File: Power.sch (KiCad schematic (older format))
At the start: 65 parts, among them J3 ESTOP, J4 PWR, J5 Conn_ARM_JTAG_SWD_10, J7 FAN, Q1 MMBT5401LT1G, Q2 Q_NMOS_GDS, Q3 MMBT3904, Q4 Q_NMOS_GDS, Q5 Q_NMOS_GDS, Q6 Q_NMOS_GDS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

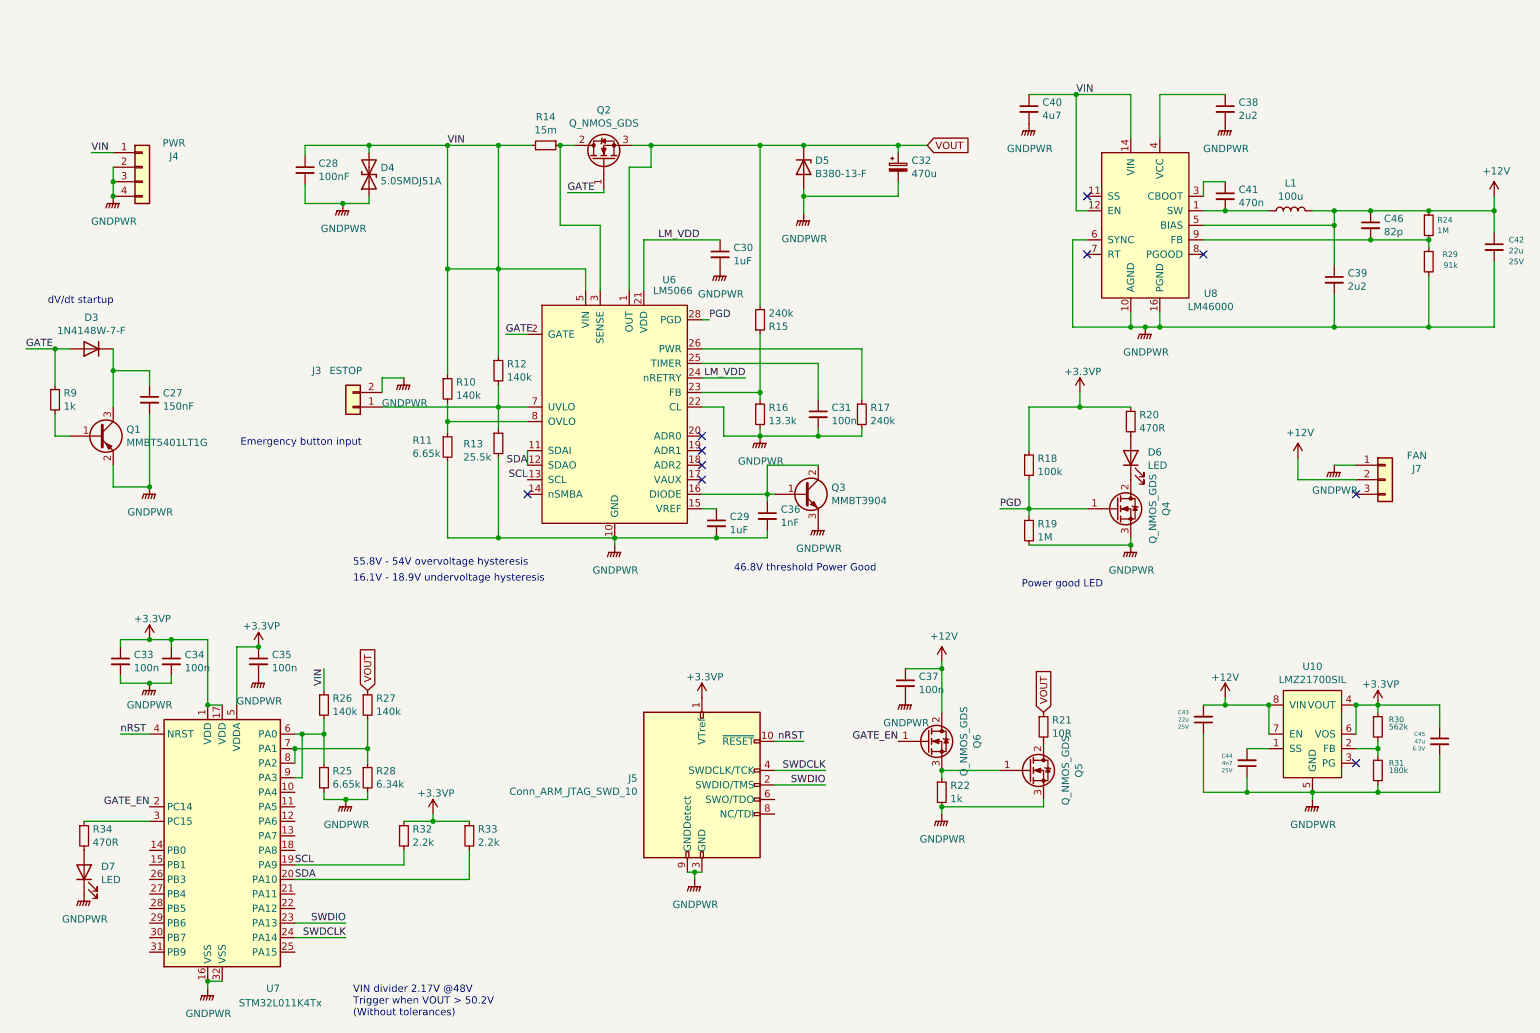
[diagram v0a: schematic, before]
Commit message: add rs485 termination, change to SOT-323 TVS diodes, various OCD
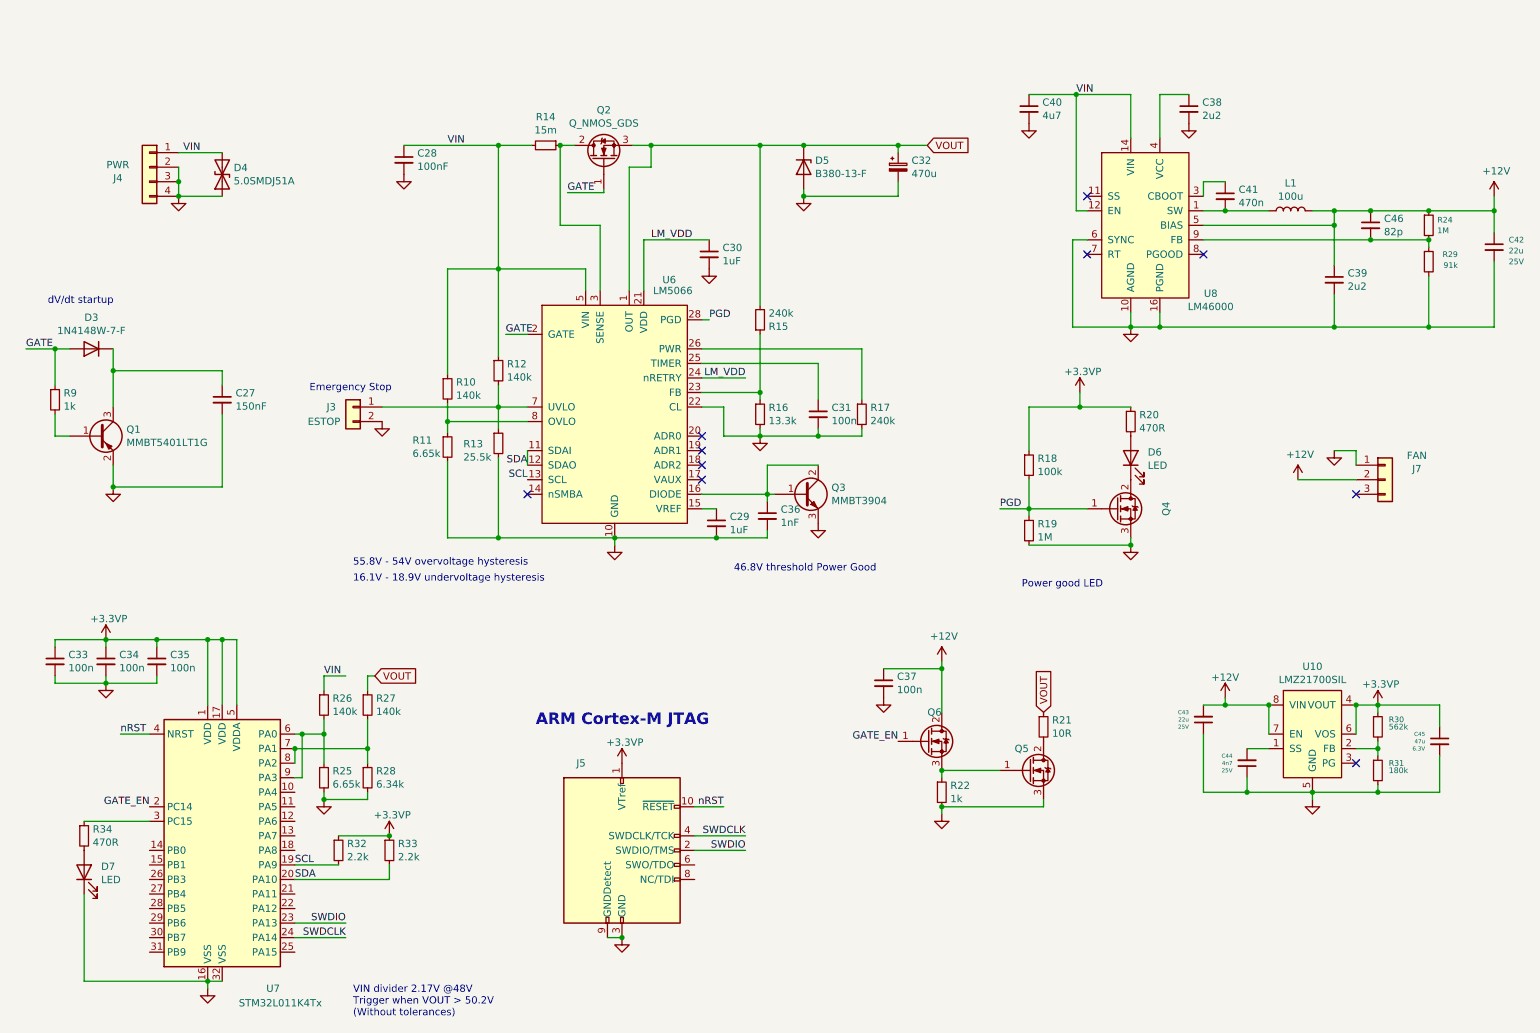
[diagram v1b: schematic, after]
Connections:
- net GNDPWR renamed GND
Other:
- note added: "ARM Cortex-M JTAG"
- note added: "Emergency Stop"
- note removed: "Emergency button input"
- moved on the sheet: C27, C28, C30, C33, C34, C35, C37, C38, D4, J3, J4, J5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

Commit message: working through the power subsystems now. changed e-stop topology.
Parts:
- removed R19: 1M, Resistor_SMD:R_0603_1608Metric, symbol Device:R_Small
- added C47: 100n, Capacitor_SMD:C_0603_1608Metric, symbol Device:C_Small
- added Q7: NTS4001NT1G, Package_TO_SOT_SMD:SOT-323_SC-70, symbol Device:Q_NMOS_GSD
- added R35: 1k, Resistor_SMD:R_0603_1608Metric, symbol Device:R_Small
- added R36: 10k, Resistor_SMD:R_0603_1608Metric, symbol Device:R_Small
- added R37: 100k, Resistor_SMD:R_0603_1608Metric, symbol Device:R_Small
- D4: value 5.0SMDJ51A -> 5.0SMDJ60A; D1N (none) -> Digikey; D1PN (none) -> 5.0SMDJ60ABBCT-ND; MFN (none) -> Bourns; MPN (none) -> 5.0SMDJ60A
- D5: symbol Device:D_Zener -> Device:D_Schottky
- J7: D1N (none) -> digikey; D1PN (none) -> WM4201-ND; MFN (none) -> Molex; MPN (none) -> 0022232031
- R11: value 6.65k -> 6k65
- R13: value 25.5k -> 25k5
- R14: D1N (none) -> Digikey; D1PN (none) -> WSLH-.015CT-ND; MFN (none) -> Vishay Dale; MPN (none) -> WSL2512R0150FEA18
- U6: D1N (none) -> Digikey; D1PN (none) -> 296-LM5066PMHX/NOPBCT-ND; MFN (none) -> TI; MPN (none) -> LM5066PMHX/NOPB
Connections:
- net +12V: now also R35.1
- net GND: now also Q1.3 (C), C47.2, Q7.2 (S), R37.2; no longer J3.2 (Pin_2), Q1.2 (E)
- net at R12.2, R13.1, U6.7 (UVLO): now also Q7.3 (D); no longer J3.1 (Pin_1)
- net at C27.1, D3.1 (K): now also Q1.2 (E); no longer Q1.3 (C)
- new net: J3.1 (Pin_1), R35.2
- new net: C47.1, J3.2 (Pin_2), R36.1
- new net: Q7.1 (G), R36.2, R37.1
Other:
- note added: "COMP1 on PA0/PA1\nCOMP2 on PA3/PA2"
- note added: "I2C addr: ZZZ = 0x40"
- note added: "Schottky diode to eat\nkickback energy at power-off"
- note added: "TODO: check FET pinouts"
- note added: "TODO: check pinout"
- note added: "With a 15 mOhm shunt,\ncurrent limit trips at 3.33 amps (nominal)"
- note added: "open-drain"
- moved on the sheet: C27, C28, C32, C36, D3, D4, D5, J3, J4, J7, Q1, Q2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

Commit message: adding a few notes
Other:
- note added: "20 uA / C27 = 0.133 V / ms ramp rate"
- note added: "TODO: check transistor pinout"
- moved on the sheet: C27, C28, C29, C30, C31, C32, C36, C43, C44, C45, C47, D3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

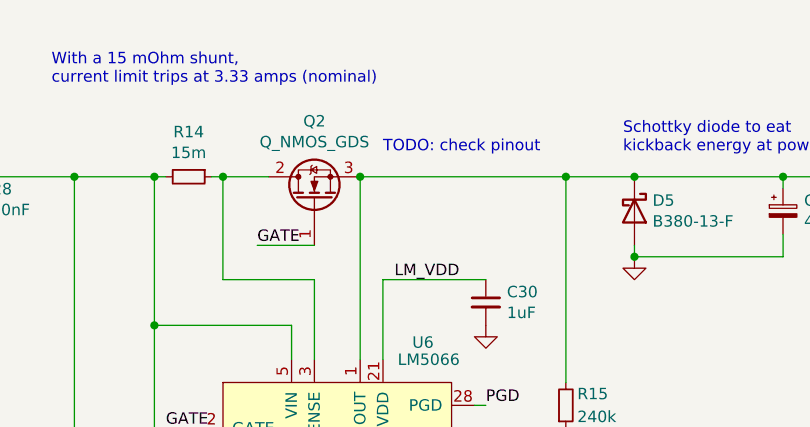
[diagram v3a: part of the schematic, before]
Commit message: add two part numbers
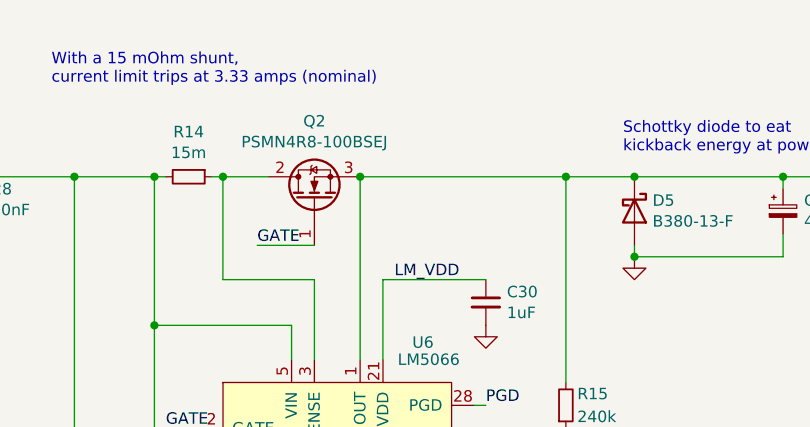
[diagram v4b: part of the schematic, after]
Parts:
- C32: D1N (none) -> Digikey; D1PN (none) -> PCE4859CT-ND; MFN (none) -> Panasonic; MPN (none) -> EEE-FK1K471AM
- D5: D1N (none) -> Digikey; D1PN (none) -> B380-FDICT-ND; MFN (none) -> Diodes Inc; MPN (none) -> B380-13-F
- Q2: value Q_NMOS_GDS -> PSMN4R8-100BSEJ; D1N (none) -> Digikey; D1PN (none) -> 1727-1103-1-ND; MFN (none) -> NXP; MPN (none) -> PSMN4R8-100BSEJ
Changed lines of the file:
@@
 Text Notes 3950 5650 2    50   ~ 0
 COMP1 on PA0/PA1\nCOMP2 on PA3/PA2
-Text Notes 4350 1600 0    50   ~ 0
-TODO: check pinout
 Text Notes 4970 4440 0    50   ~ 0
 46.8V threshold Power Good
@@
 F 2 "Capacitor_SMD:CP_Elec_18x17.5" H 6100 1850 50  0001 C CNN
 F 3 "~" H 6100 1850 50  0001 C CNN
+F 4 "Digikey" H 6100 1850 50  0001 C CNN "D1N"
+F 5 "PCE4859CT-ND" H 6100 1850 50  0001 C CNN "D1PN"
+F 6 "Panasonic" H 6100 1850 50  0001 C CNN "MFN"
+F 7 "EEE-FK1K471AM" H 6100 1850 50  0001 C CNN "MPN"
 	1    6100 1850
 	1    0    0    -1
@@
 F 2 "Diode_SMD:D_SMC" H 5450 1850 50  0001 C CNN
 F 3 "~" H 5450 1850 50  0001 C CNN
+F 4 "Digikey" V 5450 1850 50  0001 C CNN "D1N"
+F 5 "B380-FDICT-ND" V 5450 1850 50  0001 C CNN "D1PN"
+F 6 "Diodes Inc" V 5450 1850 50  0001 C CNN "MFN"
+F 7 "B380-13-F" V 5450 1850 50  0001 C CNN "MPN"
 	1    5450 1850
 	0    1    1    0
@@
 P 4050 1800
 F 0 "Q2" V 4393 1800 50  0000 C CNN
-F 1 "Q_NMOS_GDS" V 4302 1800 50  0000 C CNN
+F 1 "PSMN4R8-100BSEJ" V 4302 1800 50  0000 C CNN
 F 2 "Package_TO_SOT_SMD:TO-263-2" H 4250 1900 50  0001 C CNN
 F 3 "~" H 4050 1800 50  0001 C CNN
+F 4 "Digikey" V 4050 1800 50  0001 C CNN "D1N"
+F 5 "1727-1103-1-ND" V 4050 1800 50  0001 C CNN "D1PN"
+F 6 "NXP" V 4050 1800 50  0001 C CNN "MFN"
+F 7 "PSMN4R8-100BSEJ" V 4050 1800 50  0001 C CNN "MPN"
 	1    4050 1800
 	0    -1   -1   0

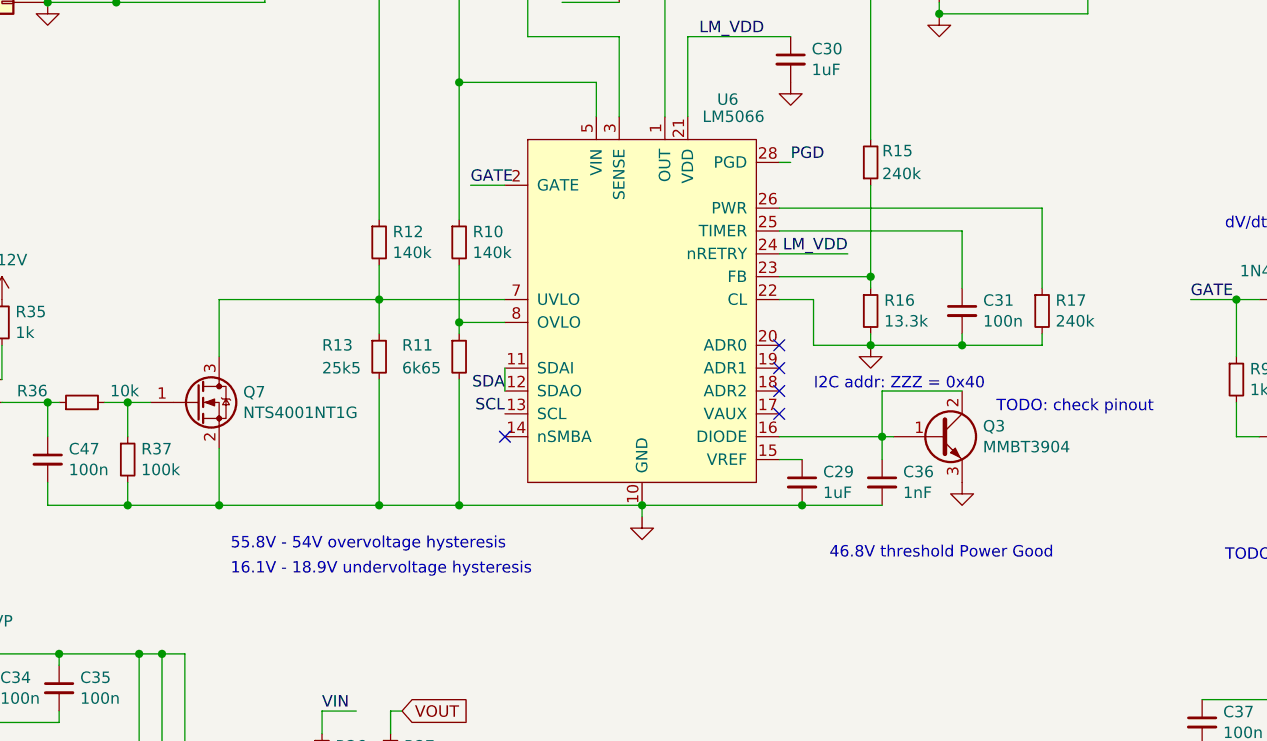
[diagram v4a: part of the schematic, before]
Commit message: recalculate lm5066 passives
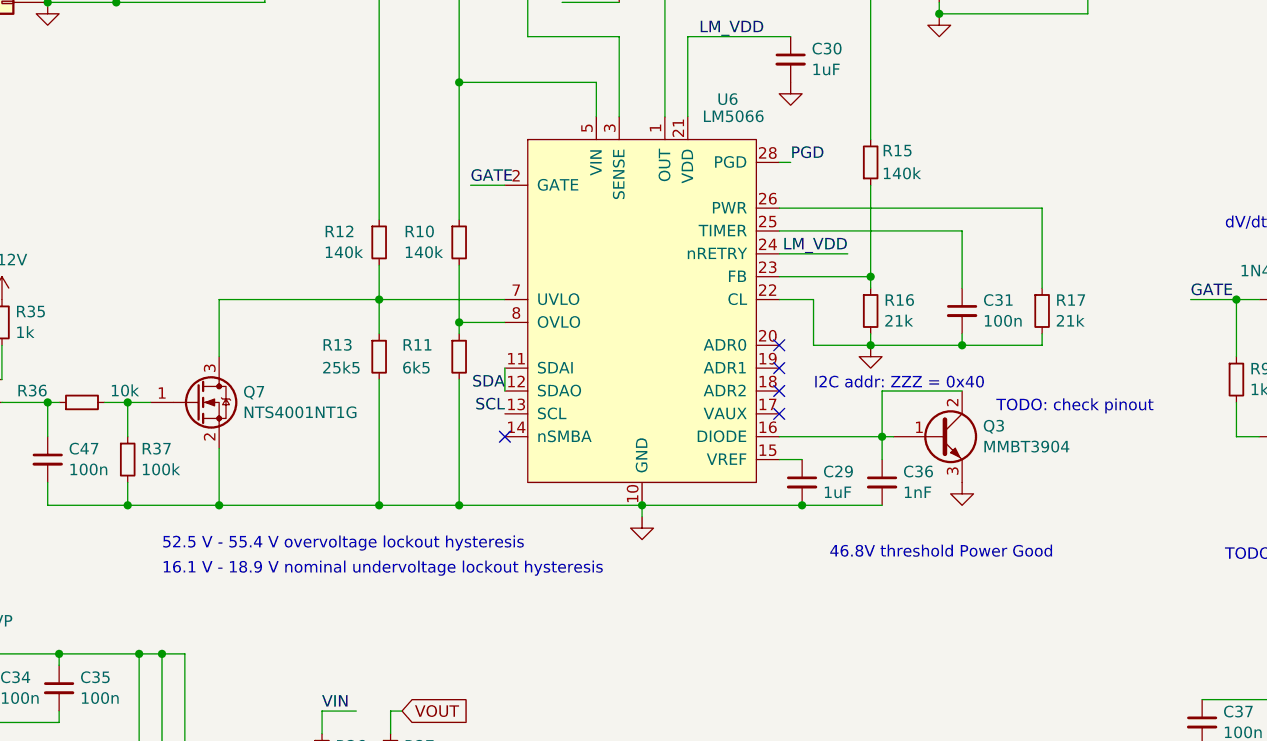
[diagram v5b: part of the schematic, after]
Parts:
- R11: value 6k65 -> 6k5
- R15: value 240k -> 140k
- R16: value 13.3k -> 21k
- R17: value 240k -> 21k
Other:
- note added: "16.1 V - 18.9 V nominal undervoltage lockout hysteresis"
- note added: "52.5 V - 55.4 V overvoltage lockout hysteresis"
- note removed: "16.1V - 18.9V undervoltage hysteresis"
- note removed: "55.8V - 54V overvoltage hysteresis"
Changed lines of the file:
@@
 Text Notes 600  3550 0    50   ~ 0
 Emergency Stop
-Text Notes 2350 4400 0    50   ~ 0
-55.8V - 54V overvoltage hysteresis
-Text Notes 2350 4510 0    50   ~ 0
-16.1V - 18.9V undervoltage hysteresis
+Text Notes 2050 4400 0    50   ~ 0
+52.5 V - 55.4 V overvoltage lockout hysteresis
+Text Notes 2050 4510 0    50   ~ 0
+16.1 V - 18.9 V nominal undervoltage lockout hysteresis
 Text Notes 2900 1300 0    50   ~ 0
 With a 15 mOhm shunt,\ncurrent limit trips at 3.33 amps (nominal)
@@
 U 1 1 5D2C7C82
 P 3000 3050
-F 0 "R12" H 3059 3096 50  0000 L CNN
-F 1 "140k" H 3059 3005 50  0000 L CNN
+F 0 "R12" H 2759 3096 50  0000 L CNN
+F 1 "140k" H 2759 3005 50  0000 L CNN
 F 2 "Resistor_SMD:R_0603_1608Metric" H 3000 3050 50  0001 C CNN
 F 3 "~" H 3000 3050 50  0001 C CNN
@@
 U 1 1 5D2C7C83
 P 3350 3050
-F 0 "R10" H 3409 3096 50  0000 L CNN
-F 1 "140k" H 3409 3005 50  0000 L CNN
+F 0 "R10" H 3109 3096 50  0000 L CNN
+F 1 "140k" H 3109 3005 50  0000 L CNN
 F 2 "Resistor_SMD:R_0603_1608Metric" H 3350 3050 50  0001 C CNN
 F 3 "~" H 3350 3050 50  0001 C CNN
@@
 P 3350 3550
 F 0 "R11" H 3100 3600 50  0000 L CNN
-F 1 "6k65" H 3100 3500 50  0000 L CNN
+F 1 "6k5" H 3100 3500 50  0000 L CNN
 F 2 "Resistor_SMD:R_0603_1608Metric" H 3350 3550 50  0001 C CNN
 F 3 "~" H 3350 3550 50  0001 C CNN
@@
 P 5150 2700
 F 0 "R15" H 5200 2650 50  0000 L CNN
-F 1 "240k" H 5200 2750 50  0000 L CNN
+F 1 "140k" H 5200 2750 50  0000 L CNN
 F 2 "Resistor_SMD:R_0603_1608Metric" H 5150 2700 50  0001 C CNN
 F 3 "~" H 5150 2700 50  0001 C CNN
@@
 P 5150 3350
 F 0 "R16" H 5209 3396 50  0000 L CNN
-F 1 "13.3k" H 5209 3305 50  0000 L CNN
+F 1 "21k" H 5209 3305 50  0000 L CNN
 F 2 "Resistor_SMD:R_0603_1608Metric" H 5150 3350 50  0001 C CNN
 F 3 "~" H 5150 3350 50  0001 C CNN
@@
 P 5900 3350
 F 0 "R17" H 5959 3396 50  0000 L CNN
-F 1 "240k" H 5959 3305 50  0000 L CNN
+F 1 "21k" H 5959 3305 50  0000 L CNN
 F 2 "Resistor_SMD:R_0603_1608Metric" H 5900 3350 50  0001 C CNN
 F 3 "~" H 5900 3350 50  0001 C CNN

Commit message: fix Q3 pinout and chase a few part numbers
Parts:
- D3: D1N (none) -> Digikey; D1PN (none) -> 1N4148W-FDICT-ND; MFN (none) -> Diodes Inc; MPN (none) -> 1N4148W-7-F
- Q1: D1N (none) -> Digikey; D1PN (none) -> MMBT5401LT1GOSCT-ND; MFN (none) -> ON Semi; MPN (none) -> MMBT5401LT1G
- Q3: symbol Device:Q_NPN_BCE -> Device:Q_NPN_BEC; D1N (none) -> Digikey; D1PN (none) -> MMBT3904-FDICT-ND; MFN (none) -> Diodes Inc; MPN (none) -> MMBT3904-7-F
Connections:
- net GND: now also Q3.2 (E); no longer Q3.3 (E)
- net at C36.1, Q3.1 (B), U6.16 (DIODE): now also Q3.3 (C); no longer Q3.2 (C)
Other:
- note added: "18.9 V threshold Power Good"
- note removed: "46.8V threshold Power Good"
- note removed: "TODO: check pinout"
- note removed: "TODO: check transistor pinout"
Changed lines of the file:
@@
 Connection ~ 5150 3500
 Connection ~ 5200 3900
+Connection ~ 5200 4200
 Connection ~ 5450 1700
 Connection ~ 5450 2050
@@
 	5200 4200 4850 4200
 Wire Wire Line
+	5200 4200 5550 4200
+Wire Wire Line
 	5250 3900 5200 3900
 Wire Wire Line
@@
 Wire Wire Line
 	5550 3700 5200 3700
+Wire Wire Line
+	5550 4100 5550 4200
 Wire Wire Line
 	5650 6200 5300 6200
@@
 COMP1 on PA0/PA1\nCOMP2 on PA3/PA2
 Text Notes 4970 4440 0    50   ~ 0
-46.8V threshold Power Good
+18.9 V threshold Power Good
 Text Notes 5400 1600 0    50   ~ 0
 Schottky diode to eat\nkickback energy at power-off
@@
 Text Notes 5650 3700 2    50   ~ 0
 I2C addr: ZZZ = 0x40
-Text Notes 5700 3800 0    50   ~ 0
-TODO: check pinout
 Text Notes 6700 3000 0    50   ~ 0
 dV/dt startup
-Text Notes 6700 4450 0    50   ~ 0
-TODO: check transistor pinout
 Text Notes 7200 6100 0    50   ~ 0
 TODO: check FET pinouts
-Text Notes 8500 4550 2    50   ~ 0
+Text Notes 8300 4450 2    50   ~ 0
 20 uA / C27 = 0.133 V / ms ramp rate
 Text Notes 9150 6150 0    50   ~ 0
@@
 $EndComp
 $Comp
-L power:GND #PWR0141
-U 1 1 5E50DF19
-P 5550 4100
-F 0 "#PWR0141" H 5550 3850 50  0001 C CNN
-F 1 "GND" H 5555 3927 50  0001 C CNN
-F 2 "" H 5550 4100 50  0001 C CNN
-F 3 "" H 5550 4100 50  0001 C CNN
-	1    5550 4100
-	-1   0    0    -1
-$EndComp
-$Comp
 L power:GND #PWR0145
 U 1 1 5E52C140
@@
 F 2 "Diode_SMD:D_SOD-123" H 7000 3300 50  0001 C CNN
 F 3 "~" H 7000 3300 50  0001 C CNN
+F 4 "Digikey" H 7000 3300 50  0001 C CNN "D1N"
+F 5 "1N4148W-FDICT-ND" H 7000 3300 50  0001 C CNN "D1PN"
+F 6 "Diodes Inc" H 7000 3300 50  0001 C CNN "MFN"
+F 7 "1N4148W-7-F" H 7000 3300 50  0001 C CNN "MPN"
 	1    7000 3300
 	-1   0    0    1
@@
 $EndComp
 $Comp
-L Device:Q_NPN_BCE Q3
+L Device:Q_NPN_BEC Q3
 U 1 1 5D2C7C9A
 P 5450 3900
@@
 F 2 "Package_TO_SOT_SMD:SOT-23" H 5650 4000 50  0001 C CNN
 F 3 "~" H 5450 3900 50  0001 C CNN
+F 4 "Digikey" H 5450 3900 50  0001 C CNN "D1N"
+F 5 "MMBT3904-FDICT-ND" H 5450 3900 50  0001 C CNN "D1PN"
+F 6 "Diodes Inc" H 5450 3900 50  0001 C CNN "MFN"
+F 7 "MMBT3904-7-F" H 5450 3900 50  0001 C CNN "MPN"
 	1    5450 3900
 	1    0    0    -1
@@
 F 2 "Package_TO_SOT_SMD:SOT-23" H 7250 4000 50  0001 C CNN
 F 3 "~" H 7050 3900 50  0001 C CNN
+F 4 "Digikey" H 7050 3900 50  0001 C CNN "D1N"
+F 5 "MMBT5401LT1GOSCT-ND" H 7050 3900 50  0001 C CNN "D1PN"
+F 6 "ON Semi" H 7050 3900 50  0001 C CNN "MFN"
+F 7 "MMBT5401LT1G" H 7050 3900 50  0001 C CNN "MPN"
 	1    7050 3900
 	1    0    0    1
